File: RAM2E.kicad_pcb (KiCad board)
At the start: 4 copper layers, 77.7 x 53 mm, 19 parts, among them J1 AppleIIeAux, U1 EPM7128SL84, U2 2M x 8

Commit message: Changed name to "RAM2E"
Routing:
- net /RD4: track 22.2 -> 23.6 mm
- net /RD3: track 19.5 -> 20.6 mm
- net /RD5: track 20.3 -> 21.1 mm
- net /RD0: track 19.5 -> 20.0 mm
- net /RD2: track 19.5 -> 20.0 mm
- net /~RAS~: track 20.0 -> 19.5 mm
- net /R~WE~: track 19.5 -> 20.0 mm
- net GND: vias 616 -> 627

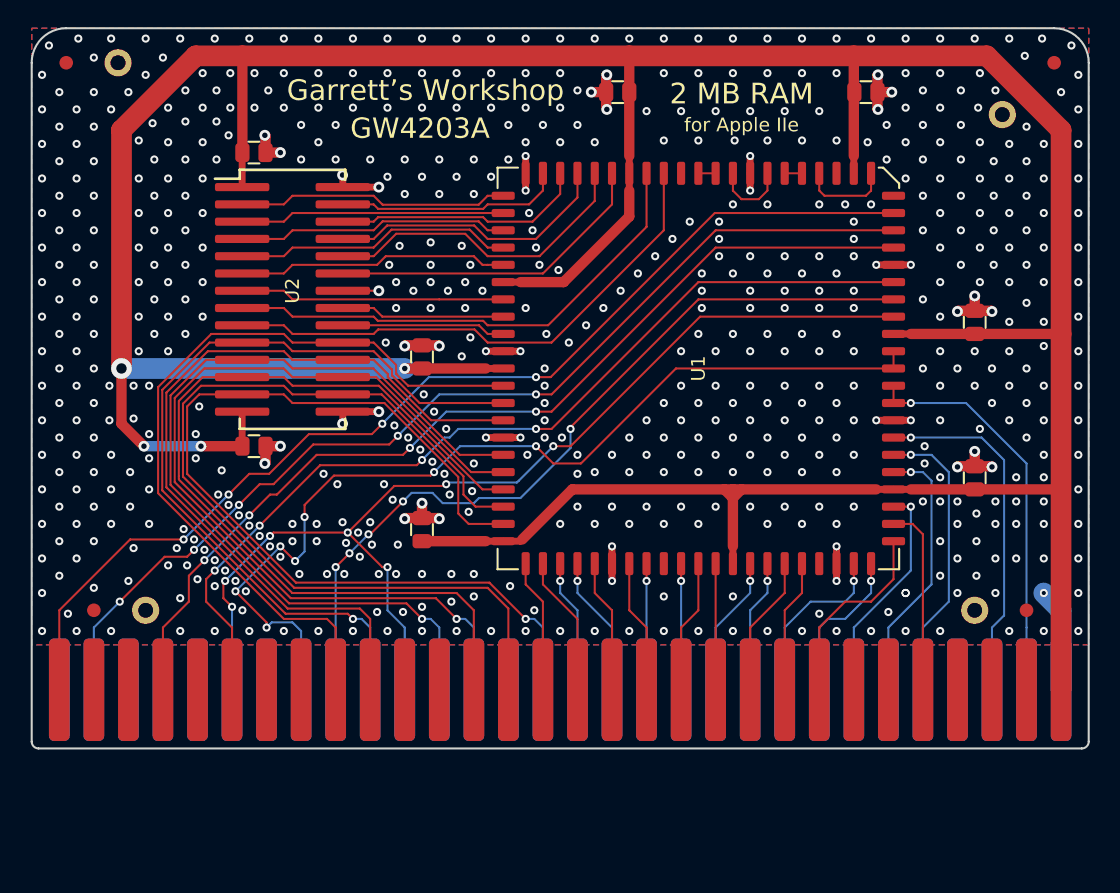
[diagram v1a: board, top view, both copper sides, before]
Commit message: halfway done widening clearances
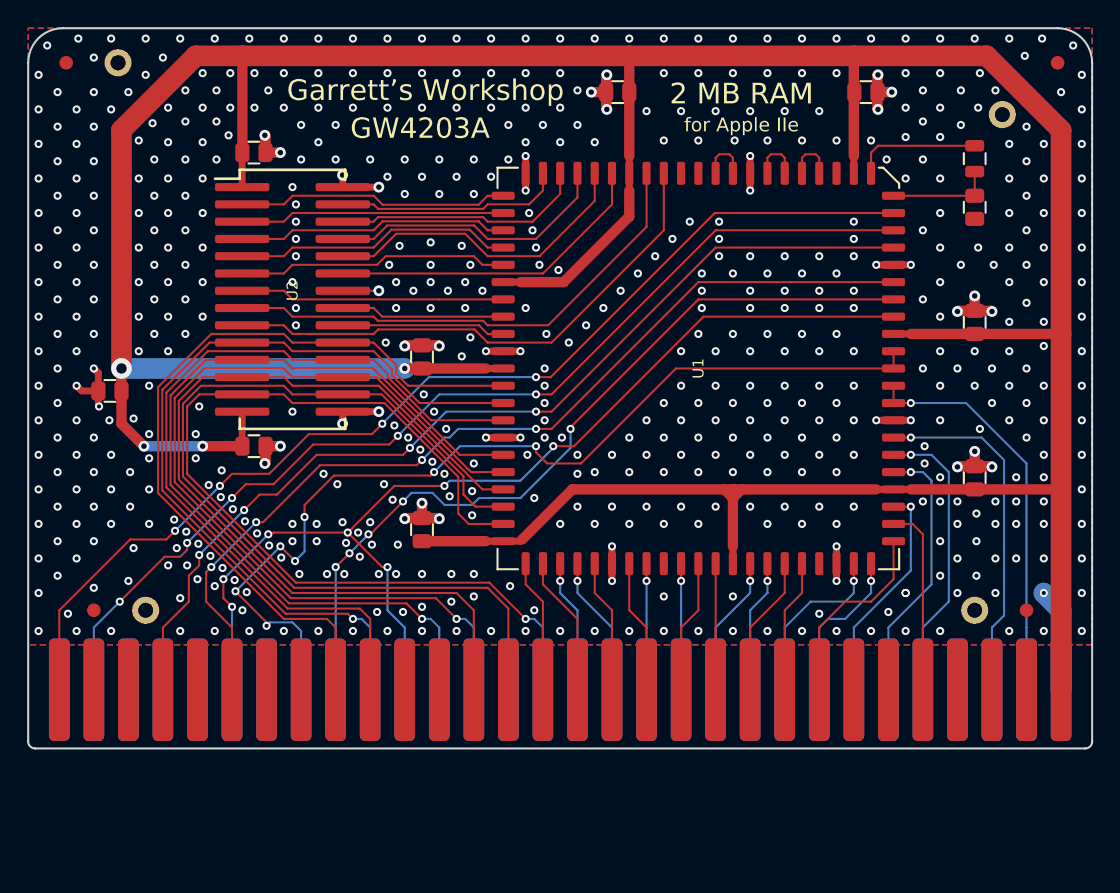
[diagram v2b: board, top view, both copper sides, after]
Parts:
- added C2: 100n, stdpads:C_0805, F.Cu at (204.4, 113.4)
- added C9: 10p, stdpads:C_0805, F.Cu at (268.0, 99.9)
- added R1: 820, stdpads:R_0805, F.Cu at (268.0, 96.3)
- U2: value 2M x 8 -> DRAM_2Mx8
- moved FID3 0.25 mm to (274.1, 89.3)
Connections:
- U1 pad 12: Net-(U1-Pad12) -> Net-(R1-Pad1)
- U1 pad 15: Net-(U1-Pad12) -> Net-(U1-Pad15)
- U1 pad 16: Net-(U1-Pad16) -> Net-(U1-Pad15)
- U1 pad 17: Net-(U1-Pad16) -> Net-(U1-Pad17)
- U1 pad 18: Net-(U1-Pad18) -> Net-(U1-Pad17)
- U1 pad 20: Net-(U1-Pad18) -> Net-(U1-Pad20)
- U1 pad 21: Net-(U1-Pad21) -> Net-(U1-Pad20)
- U1 pad 22: Net-(U1-Pad21) -> Net-(U1-Pad22)
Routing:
- net Net-(R1-Pad1): track 0.00 -> 9.35 mm
- net Net-(C9-Pad1): track 0.00 -> 7.75 mm
- net Net-(U1-Pad12): track 6.66 -> 0.00 mm
- net Net-(U1-Pad18): track 5.60 -> 0.00 mm
- net GND: track 63.3 -> 68.0 mm, vias 627 -> 618
- net Net-(U1-Pad20): track 0.00 -> 3.77 mm
- net Net-(U1-Pad17): track 0.00 -> 3.77 mm
- net Net-(U1-Pad15): track 0.00 -> 3.77 mm
- net Net-(U1-Pad16): track 1.27 -> 0.00 mm
- net Net-(U1-Pad21): track 1.27 -> 0.00 mm
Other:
- board size 77.7 x 53 mm -> 78.2 x 53 mm
- copper layers 4 -> 2
- rule solder_mask_min_width: 0.1524 -> 0.127

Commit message: Finished new revision 0.6
Wider clearance and 1 more bypass cap
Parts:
- renumbered C2 to C10

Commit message: Schematic documentation update
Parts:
- C1, C10, C2, C3, C4, C5, C6, C7, C8: value 100n -> 10u
- R1: value 820 -> 1k2
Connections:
- net /14M renamed /C14M
- net /3.58M renamed /C3M58
- net /7M renamed /C7M
- net /RA0 renamed /MA0
- net /RA1 renamed /MA1
- net /RA2 renamed /MA2
- net /RA3 renamed /MA3
- net /RA4 renamed /MA4
- net /RA5 renamed /MA5
- net /RA6 renamed /MA6
- net /RA7 renamed /MA7
- net /V0 renamed /VD0
- net /V1 renamed /VD1
- net /V2 renamed /VD2
- net /V3 renamed /VD3
- net /V4 renamed /VD4
- net /V5 renamed /VD5
- net /V6 renamed /VD6
- net /V7 renamed /VD7

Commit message: more
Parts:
- removed C1, C10, C2, C3, C4, C5, C6, C7, C8: 10u, stdpads:C_0805
- removed C9: 10p, stdpads:C_0805
- removed H3: , stdpads:PasteHole_1.1mm_PTH
- removed the H4 at (268.0, 129.5)
- removed R1: 1k2, stdpads:R_0805
- added H4: , stdpads:PasteHole_1.1mm_PTH, F.Cu at (274.3, 125.9)
- added H4: , stdpads:PasteHole_1.1mm_PTH, F.Cu at (274.1, 92.8)
- added H4: , stdpads:PasteHole_1.1mm_PTH, F.Cu at (274.3, 128.4)
- added REF**: Tag-Connect_TC2050-IDC-FP_2x05_P1.27mm_Vertical, Connector:Tag-Connect_TC2050-IDC-FP_2x05_P1.27mm_Vertical, F.Cu at (206.8, 115.6)
- added REF**: C_0805, stdpads:C_0805, F.Cu at (262.3, 111.5)
- added REF**: C_0805, stdpads:C_0805, F.Cu at (262.2, 108.7)
- added REF**: R_0805, stdpads:R_0805, F.Cu at (271.3, 112.8)
- added REF**: R_0805, stdpads:R_0805, F.Cu at (271.3, 116.2)
- added REF**: C_0805, stdpads:C_0805, F.Cu at (271.3, 119.6)
- added REF**: C_0805, stdpads:C_0805, F.Cu at (271.3, 107.4)
- added REF**: R_0805, stdpads:R_0805, F.Cu at (271.3, 100.6)
- added REF**: R_0805, stdpads:R_0805, F.Cu at (271.3, 104.0)
- added REF**: R_0805, stdpads:R_0805, F.Cu at (228.3, 118.7)
- added REF**: C_0603, stdpads:C_0603, F.Cu at (225.6, 122.4)
- added REF**: C_0603, stdpads:C_0603, F.Cu at (223.8, 93.3)
- added REF**: AppleIIeAux_Edge, stdpads:AppleIIeAux_Edge, F.Cu at (237.5, 135.4)
- added REF**: C_0603, stdpads:C_0603, F.Cu at (216.3, 122.4)
- added REF**: C_0603, stdpads:C_0603, F.Cu at (253.2, 122.4)
- added REF**: C_0603, stdpads:C_0603, F.Cu at (243.9, 122.4)
- added REF**: C_0603, stdpads:C_0603, F.Cu at (234.8, 122.4)
- added REF**: C_0603, stdpads:C_0603, F.Cu at (226.6, 99.8)
- added REF**: C_0603, stdpads:C_0603, F.Cu at (211.0, 104.7)
- added REF**: C_0603, stdpads:C_0603, F.Cu at (230.3, 107.8)
- added REF**: C_0603, stdpads:C_0603, F.Cu at (249.8, 107.8)
- added REF**: C_0603, stdpads:C_0603, F.Cu at (236.8, 118.0)
- added REF**: C_0603, stdpads:C_0603, F.Cu at (223.8, 117.5)
- added REF**: C_0603, stdpads:C_0603, F.Cu at (243.8, 118.0)
- added REF**: C_0603, stdpads:C_0603, F.Cu at (244.3, 98.7)
- added REF**: C_0603, stdpads:C_0603, F.Cu at (237.3, 98.7)
- added REF**: C_0603, stdpads:C_0603, F.Cu at (213.8, 93.3)
- added REF**: C_0603, stdpads:C_0603, F.Cu at (211.0, 95.9)
- added REF**: C_0603, stdpads:C_0603, F.Cu at (211.0, 100.7)
- added REF**: C_0603, stdpads:C_0603, F.Cu at (226.6, 104.6)
- added REF**: C_0603, stdpads:C_0603, F.Cu at (213.8, 117.5)
- added REF**: C_0805, stdpads:C_0805, F.Cu at (254.4, 97.4)
- added REF**: R_0805, stdpads:R_0805, F.Cu at (251.1, 97.4)
- added REF**: C_0603, stdpads:C_0603, F.Cu at (230.5, 116.2)
- added REF**: C_0603, stdpads:C_0603, F.Cu at (250.2, 111.5)
- added REF**: C_0805, stdpads:C_0805, F.Cu at (265.7, 111.5)
- added REF**: C_0805, stdpads:C_0805, F.Cu at (265.7, 108.7)
- added U3: TSSOP-20_4.4x6.5mm_P0.65mm, Package_SO:TSSOP-20_4.4x6.5mm_P0.65mm, F.Cu at (220.8, 124.6)
- added U4: TSSOP-20_4.4x6.5mm_P0.65mm, Package_SO:TSSOP-20_4.4x6.5mm_P0.65mm, F.Cu at (230.0, 124.6)
- added U5: TSSOP-20_4.4x6.5mm_P0.65mm, Package_SO:TSSOP-20_4.4x6.5mm_P0.65mm, F.Cu at (239.2, 124.6)
- added U6: TSSOP-20_4.4x6.5mm_P0.65mm, Package_SO:TSSOP-20_4.4x6.5mm_P0.65mm, F.Cu at (248.4, 124.6)
- added U7: TSSOP-20_4.4x6.5mm_P0.65mm, Package_SO:TSSOP-20_4.4x6.5mm_P0.65mm, F.Cu at (257.6, 124.6)
- added U8: SOT-223-6, stdpads:SOT-223-6, F.Cu at (265.2, 116.2)
- added U9: SOT-223-6, stdpads:SOT-223-6, F.Cu at (265.2, 104.0)
- U1: value EPM7128SL84 -> TQFP-100_14x14mm_P0.5mm; footprint stdpads:PLCC-84 -> Package_QFP:TQFP-100_14x14mm_P0.5mm
- U2: value DRAM_2Mx8 -> TSOP-II-54_22.2x10.16mm_P0.8mm; footprint stdpads:SOJ-28-300mil -> stdpads:TSOP-II-54_22.2x10.16mm_P0.8mm
- moved J1 9.14 mm to (237.5, 144.5)
- moved U1 8.33 mm to (240.1, 108.3), turned to 0 degrees
- moved H1 6.35 mm to (200.7, 129.5)
- moved H2 5.40 mm to (200.9, 92.8)
- moved FID3 4.37 mm to (271.5, 92.8)
- moved FID2 4.23 mm to (203.5, 92.8)
- moved FID4 1.94 mm to (270.1, 128.5)
- moved U2 1.58 mm to (218.8, 105.5)
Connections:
- U1 pad 1: /Q3 -> (no net)
- U1 pad 10: /C3M58 -> GND
- U1 pad 11: Net-(C9-Pad1) -> GND
- U1 pad 12: Net-(R1-Pad1) -> (no net)
- U1 pad 13: +5V -> (no net)
- U1 pad 14: Net-(U1-Pad14) -> (no net)
- U1 pad 15: Net-(U1-Pad15) -> (no net)
- U1 pad 16: Net-(U1-Pad15) -> (no net)
- U1 pad 17: Net-(U1-Pad17) -> (no net)
- U1 pad 18: Net-(U1-Pad17) -> (no net)
- U1 pad 19: GND -> (no net)
- U1 pad 2: /Q3 -> (no net)
- U1 pad 20: Net-(U1-Pad20) -> (no net)
- U1 pad 21: Net-(U1-Pad20) -> (no net)
- U1 pad 22: Net-(U1-Pad22) -> (no net)
- U1 pad 23: Net-(U1-Pad23) -> (no net)
- U1 pad 24: /RA10 -> (no net)
- U1 pad 25: /RA11 -> (no net)
- U1 pad 26: +5V -> (no net)
- U1 pad 27: /~CAS~ -> (no net)
- U1 pad 28: /RD4 -> (no net)
- U1 pad 29: /RD5 -> (no net)
- U1 pad 3: +5V -> (no net)
- U1 pad 30: /RD6 -> (no net)
- U1 pad 31: /RD7 -> (no net)
- U1 pad 33: /RD0 -> (no net)
- U1 pad 34: /RD1 -> (no net)
- U1 pad 35: /RD2 -> (no net)
- U1 pad 36: /RD3 -> (no net)
- U1 pad 37: /R~WE~ -> (no net)
- U1 pad 38: +5V -> (no net)
- U1 pad 39: /~RAS~ -> (no net)
- U1 pad 4: /AN3 -> (no net)
- U1 pad 40: /RA9 -> (no net)
- U1 pad 41: /RA8 -> (no net)
- U1 pad 42: GND -> (no net)
- U1 pad 43: +5V -> (no net)
- U1 pad 44: /MA7 -> (no net)
- U1 pad 45: /MA0 -> (no net)
- U1 pad 46: /MA1 -> GND
- U1 pad 47: GND -> (no net)
- U1 pad 48: /MA2 -> (no net)
- U1 pad 49: /MA3 -> (no net)
- U1 pad 5: /R~W~ -> (no net)
- U1 pad 50: /MA4 -> (no net)
- U1 pad 51: /MA5 -> (no net)
- U1 pad 52: /MA6 -> (no net)
- U1 pad 53: +5V -> (no net)
- U1 pad 54: /VD7 -> (no net)
- U1 pad 55: /MD7 -> (no net)
- U1 pad 56: /VD0 -> (no net)
- U1 pad 57: /MD0 -> (no net)
- U1 pad 58: /MD6 -> (no net)
- U1 pad 59: GND -> (no net)
- U1 pad 6: /~C07X~ -> (no net)
- U1 pad 60: /VD6 -> GND
- U1 pad 61: /MD1 -> (no net)
- U1 pad 62: Net-(U1-Pad62) -> (no net)
- U1 pad 63: /VD1 -> (no net)
- U1 pad 64: /VD5 -> (no net)
- U1 pad 65: /MD5 -> GND
- U1 pad 66: +5V -> (no net)
- U1 pad 67: /VD2 -> (no net)
- U1 pad 68: /MD2 -> (no net)
- U1 pad 69: /MD4 -> (no net)
- U1 pad 7: GND -> (no net)
- U1 pad 70: /VD4 -> (no net)
- U1 pad 71: Net-(U1-Pad71) -> (no net)
- U1 pad 72: GND -> (no net)
- U1 pad 73: /MD3 -> (no net)
- U1 pad 74: /VD3 -> (no net)
- U1 pad 75: /PHI0 -> (no net)
- U1 pad 76: /~EN80~ -> (no net)
- U1 pad 77: /~CASEN~ -> (no net)
- U1 pad 78: +5V -> (no net)
- U1 pad 79: /PHI1 -> GND
- U1 pad 8: /~PRAS~ -> (no net)
- U1 pad 80: /R~W~80 -> (no net)
- U1 pad 81: /~PCAS~ -> (no net)
- U1 pad 82: GND -> (no net)
- U1 pad 83: /C14M -> (no net)
- U1 pad 84: /C14M -> (no net)
- U1 pad 9: /C7M -> (no net)
- U2 pad 1: +5V -> (no net)
- U2 pad 10: /MA0 -> (no net)
- U2 pad 11: /MA2 -> (no net)
- U2 pad 12: /MA4 -> GND
- U2 pad 13: /MA6 -> (no net)
- U2 pad 14: +5V -> (no net)
- U2 pad 15: GND -> (no net)
- U2 pad 16: /MA5 -> (no net)
- U2 pad 17: /MA3 -> (no net)
- U2 pad 18: /MA1 -> (no net)
- U2 pad 19: /MA7 -> (no net)
- U2 pad 2: /RD0 -> (no net)
- U2 pad 20: /RA8 -> (no net)
- U2 pad 21: /RA9 -> (no net)
- U2 pad 22: GND -> (no net)
- U2 pad 23: /~CAS~ -> (no net)
- U2 pad 24: /RD4 -> (no net)
- U2 pad 25: /RD5 -> (no net)
- U2 pad 26: /RD6 -> (no net)
- U2 pad 27: /RD7 -> (no net)
- U2 pad 3: /RD1 -> (no net)
- U2 pad 4: /RD2 -> (no net)
- U2 pad 5: /RD3 -> (no net)
- U2 pad 6: /R~WE~ -> GND
- U2 pad 7: /~RAS~ -> (no net)
- U2 pad 8: /RA11 -> (no net)
- U2 pad 9: /RA10 -> (no net)
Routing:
- net (no net): track 0.00 -> 2596.8 mm, vias 0 -> 211
- net GND: track 68.0 -> 162.5 mm, vias 618 -> 272
- net /C3M58: track 79.3 -> 0.00 mm, vias 4 -> 0
- net /AN3: track 79.1 -> 0.00 mm, vias 7 -> 0
- net /C7M: track 75.8 -> 0.00 mm, vias 5 -> 0
- net +5V: track 285.8 -> 213.6 mm, vias 4 -> 12
- net /~PRAS~: track 71.4 -> 0.00 mm, vias 4 -> 0
- net /Q3: track 71.4 -> 0.00 mm, vias 7 -> 0
- net /MA6: track 69.5 -> 0.00 mm, vias 1 -> 0
- net /~C07X~: track 68.8 -> 0.00 mm, vias 4 -> 0
- net /MA5: track 67.8 -> 0.00 mm
- net /MA3: track 65.4 -> 0.00 mm, vias 1 -> 0
- net /MA4: track 65.3 -> 0.00 mm
- net /MA2: track 63.7 -> 0.00 mm, vias 1 -> 0
- net /MA0: track 60.0 -> 0.00 mm, vias 1 -> 0
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- added copper zone on In2.Cu, net +5V
- added copper zone on In1.Cu, net GND
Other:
- board size 78.2 x 53 mm -> 78.2 x 49.4 mm
- copper layers 2 -> 4
- net class Default: clearance 0.1524 -> 0.15; trace_width 0.1524 -> 0.15; via_dia 0.6 -> 0.5; via_drill 0.3 -> 0.2
- rule trace_clearance: 0.1524 -> 0.15
- rule trace_min: 0.1524 -> 0.15
- rule via_min_size: 0.508 -> 0.5
- board text added: "4301B"
- board text added: "8 MB RAM"
- board text removed: "2 MB RAM"
- board text removed: "4203A"
